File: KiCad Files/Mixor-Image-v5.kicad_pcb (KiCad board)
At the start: 2 copper layers, 60.6 x 46 mm, 83 parts, among them J1 Conn_01x03_Male, J2 Conn_01x03_Female, J3 Conn_01x03_Male, J4 Conn_01x03_Female, U1 TL072, U2 TL072

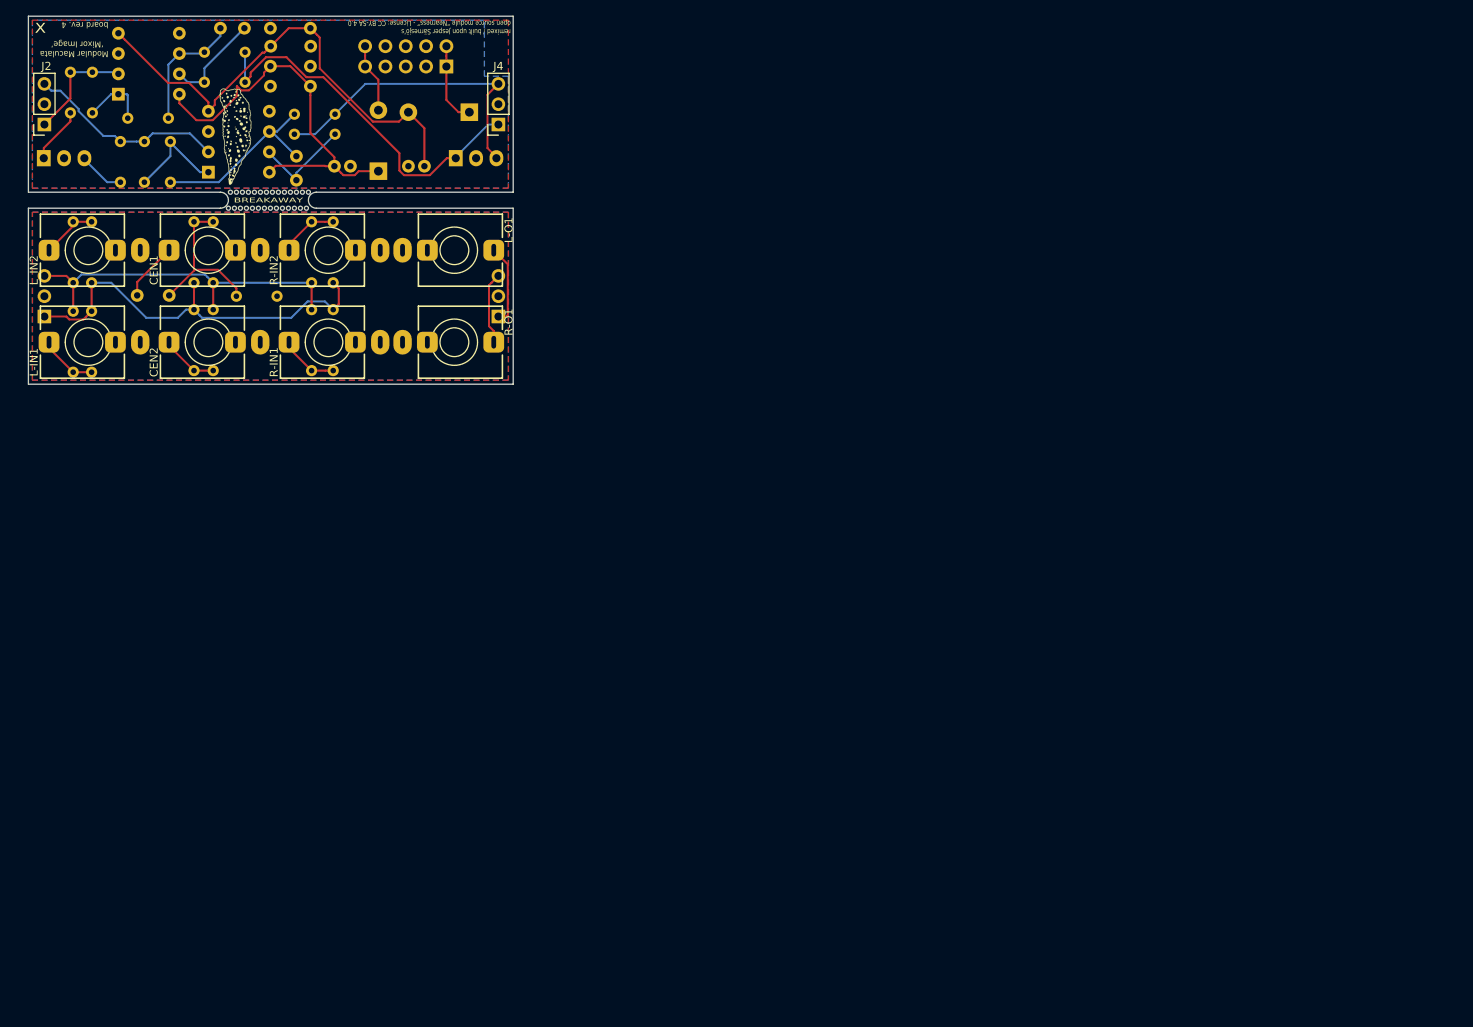
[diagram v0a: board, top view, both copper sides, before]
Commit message: remove Modular Maculata graphics
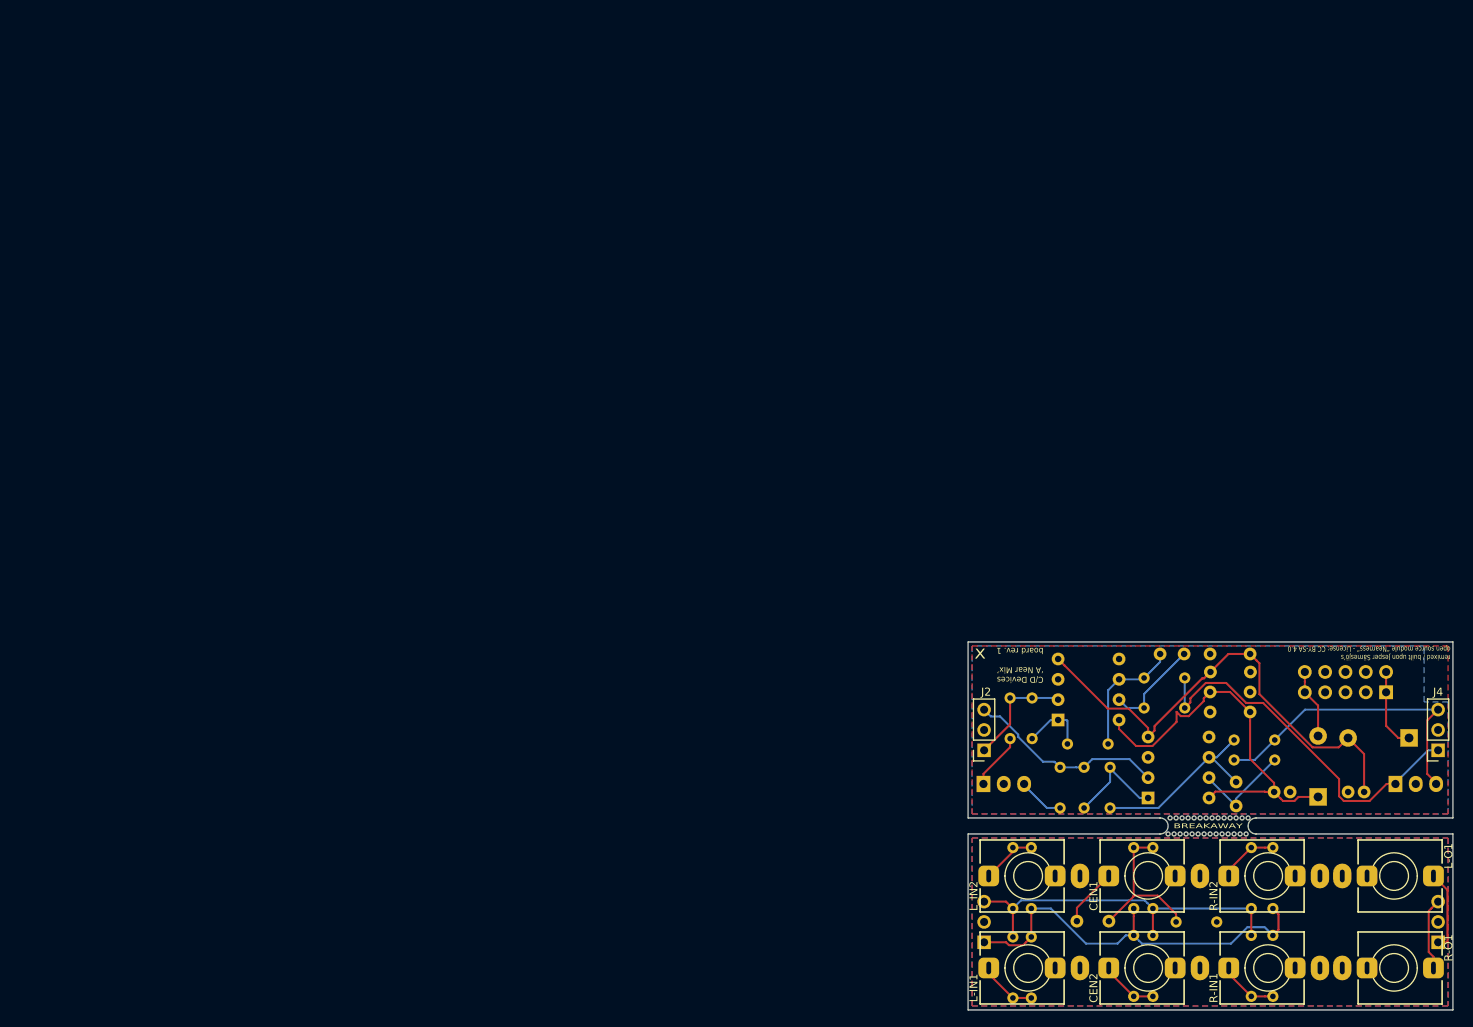
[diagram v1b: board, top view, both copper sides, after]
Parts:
- removed G*** (x2): LOGO, Nearness 1U:maculata_leaf_silk
- removed G*** (x2): LOGO, Nearness 1U:maculata_logo_copper
- removed the REF** at (25.0, 24.0)
- removed the REF** at (31.8, 24.0)
- removed the REF** at (32.5, 24.0)
- removed the REF** at (33.2, 24.0)
- removed the REF** at (34.0, 24.0)
- removed the REF** at (34.8, 24.0)
- removed the REF** at (35.0, 22.0)
- removed the REF** at (34.2, 22.0)
- removed the REF** at (33.5, 22.0)
- removed the REF** at (32.8, 22.0)
- removed the REF** at (32.0, 22.0)
- removed the REF** at (25.8, 24.0)
- removed the REF** at (31.2, 22.0)
- removed the REF** at (30.5, 22.0)
- removed the REF** at (29.8, 22.0)
- removed the REF** at (29.0, 22.0)
- removed the REF** at (28.2, 22.0)
- removed the REF** at (27.5, 22.0)
- removed the REF** at (26.8, 22.0)
- removed the REF** at (26.0, 22.0)
- removed the REF** at (26.5, 24.0)
- removed the REF** at (27.2, 24.0)
- removed the REF** at (28.0, 24.0)
- removed the REF** at (28.8, 24.0)
- removed the REF** at (29.5, 24.0)
- removed the REF** at (30.2, 24.0)
- removed the REF** at (31.0, 24.0)
- added REF**: 0.5mm_Hole, MountingHole:MountingHole_0.5mm, F.Cu at (143.2, 102.2)
- added REF**: 0.5mm_Hole, MountingHole:MountingHole_0.5mm, F.Cu at (147.0, 102.2)
- added REF**: 0.5mm_Hole, MountingHole:MountingHole_0.5mm, F.Cu at (145.7, 100.2)
- added REF**: 0.5mm_Hole, MountingHole:MountingHole_0.5mm, F.Cu at (151.7, 100.2)
- added REF**: 0.5mm_Hole, MountingHole:MountingHole_0.5mm, F.Cu at (144.7, 102.2)
- added REF**: 0.5mm_Hole, MountingHole:MountingHole_0.5mm, F.Cu at (149.5, 100.2)
- added REF**: 0.5mm_Hole, MountingHole:MountingHole_0.5mm, F.Cu at (145.0, 100.2)
- added REF**: 0.5mm_Hole, MountingHole:MountingHole_0.5mm, F.Cu at (151.0, 100.2)
- added REF**: 0.5mm_Hole, MountingHole:MountingHole_0.5mm, F.Cu at (146.2, 102.2)
- added REF**: 0.5mm_Hole, MountingHole:MountingHole_0.5mm, F.Cu at (148.0, 100.2)
- added REF**: 0.5mm_Hole, MountingHole:MountingHole_0.5mm, F.Cu at (142.5, 102.2)
- added REF**: 0.5mm_Hole, MountingHole:MountingHole_0.5mm, F.Cu at (148.7, 100.2)
- added REF**: 0.5mm_Hole, MountingHole:MountingHole_0.5mm, F.Cu at (146.5, 100.2)
- added REF**: 0.5mm_Hole, MountingHole:MountingHole_0.5mm, F.Cu at (147.2, 100.2)
- added REF**: 0.5mm_Hole, MountingHole:MountingHole_0.5mm, F.Cu at (152.5, 100.2)
- added REF**: 0.5mm_Hole, MountingHole:MountingHole_0.5mm, F.Cu at (150.2, 100.2)
- added REF**: 0.5mm_Hole, MountingHole:MountingHole_0.5mm, F.Cu at (149.2, 102.2)
- added REF**: 0.5mm_Hole, MountingHole:MountingHole_0.5mm, F.Cu at (150.7, 102.2)
- added REF**: 0.5mm_Hole, MountingHole:MountingHole_0.5mm, F.Cu at (151.5, 102.2)
- added REF**: 0.5mm_Hole, MountingHole:MountingHole_0.5mm, F.Cu at (147.7, 102.2)
- added REF**: 0.5mm_Hole, MountingHole:MountingHole_0.5mm, F.Cu at (143.5, 100.2)
- added REF**: 0.5mm_Hole, MountingHole:MountingHole_0.5mm, F.Cu at (150.0, 102.2)
- added REF**: 0.5mm_Hole, MountingHole:MountingHole_0.5mm, F.Cu at (148.5, 102.2)
- added REF**: 0.5mm_Hole, MountingHole:MountingHole_0.5mm, F.Cu at (145.5, 102.2)
- added REF**: 0.5mm_Hole, MountingHole:MountingHole_0.5mm, F.Cu at (152.2, 102.2)
- added REF**: 0.5mm_Hole, MountingHole:MountingHole_0.5mm, F.Cu at (144.0, 102.2)
- added REF**: 0.5mm_Hole, MountingHole:MountingHole_0.5mm, F.Cu at (144.2, 100.2)
- moved C1 141.1 mm to (131.1, 113.1)
- moved C2 141.1 mm to (141.5, 79.7)
- moved C3 141.1 mm to (151.0, 95.7)
- moved C4 141.1 mm to (155.7, 97.0)
- moved C5 141.1 mm to (165.0, 97.0)
- moved C6 141.1 mm to (152.7, 87.0)
- moved C7 141.1 mm to (152.8, 82.0)
- moved C8 141.1 mm to (147.7, 84.5)
- moved C9 141.1 mm to (147.7, 79.7)
- moved CEN1 141.1 mm to (140.0, 107.5)
- moved CEN2 141.1 mm to (140.0, 119.0)
- moved D1 141.1 mm to (161.2, 97.6)
- moved D2 141.1 mm to (172.6, 90.2)
- moved J1 141.1 mm to (119.5, 115.8)
- moved J2 141.1 mm to (119.5, 91.8)
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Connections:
- J1 pad 1: Net-(J1-Pad1) -> Net-(J1-Pin_1)
- J1 pad 3: Net-(J1-Pad3) -> Net-(J1-Pin_3)
- J3 pad 1: Net-(J3-Pad1) -> Net-(J3-Pin_1)
- J3 pad 3: Net-(J3-Pad3) -> Net-(J3-Pin_3)
- J4 pad 1: Net-(J4-Pad1) -> Net-(J4-Pin_1)
- J4 pad 3: Net-(J4-Pad3) -> Net-(J4-Pin_3)
- L-O1 pad T: Net-(J3-Pad1) -> Net-(J3-Pin_3)
- L-O1 pad TN: Net-(L-O1-PadTN) -> unconnected-(L-O1-PadTN)
- R-O1 pad T: Net-(J3-Pad3) -> Net-(J3-Pin_1)
- R-O1 pad TN: Net-(R-O1-PadTN) -> unconnected-(R-O1-PadTN)
- R10 pad 2: Net-(J1-Pad1) -> Net-(J1-Pin_3)
- R11 pad 2: Net-(J1-Pad3) -> Net-(J1-Pin_1)
- R12 pad 2: Net-(J1-Pad1) -> Net-(J1-Pin_3)
- R13 pad 2: Net-(J1-Pad3) -> Net-(J1-Pin_1)
- R14 pad 2: Net-(R14-Pad2) -> Net-(ST-IN1-Pin_3)
- R15 pad 1: Net-(R15-Pad1) -> Net-(ST-IN1-Pin_1)
- R2 pad 2: Net-(J1-Pad1) -> Net-(J1-Pin_3)
- R20 pad 2: Net-(J4-Pad1) -> Net-(J4-Pin_1)
- R21 pad 2: Net-(J4-Pad3) -> Net-(J4-Pin_3)
- R22 pad 2: Net-(J4-Pad1) -> Net-(J4-Pin_1)
- R23 pad 2: Net-(J4-Pad3) -> Net-(J4-Pin_3)
- R3 pad 2: Net-(J1-Pad3) -> Net-(J1-Pin_1)
- R4 pad 2: Net-(J1-Pad1) -> Net-(J1-Pin_3)
- R5 pad 2: Net-(J1-Pad3) -> Net-(J1-Pin_1)
- R6 pad 2: Net-(J1-Pad1) -> Net-(J1-Pin_3)
- R7 pad 2: Net-(J1-Pad3) -> Net-(J1-Pin_1)
- R8 pad 2: Net-(J1-Pad1) -> Net-(J1-Pin_3)
- R9 pad 2: Net-(J1-Pad3) -> Net-(J1-Pin_1)
- ST-IN1 pad 1: Net-(R14-Pad2) -> Net-(ST-IN1-Pin_1)
- ST-IN1 pad 3: Net-(R15-Pad1) -> Net-(ST-IN1-Pin_3)
- ST-OUT1 pad 1: Net-(J4-Pad1) -> Net-(J4-Pin_3)
- ST-OUT1 pad 3: Net-(J4-Pad3) -> Net-(J4-Pin_1)
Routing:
- net (no net): track 0.00 -> 213.9 mm
- net Net-(J1-Pad1): track 51.5 -> 0.00 mm
- net Net-(J4-Pad1): track 47.1 -> 0.00 mm
- net Net-(J1-Pad3): track 44.9 -> 0.00 mm
- net Net-(J4-Pad3): track 38.4 -> 0.00 mm
- net Net-(J3-Pad1): track 10.1 -> 0.00 mm
- net Net-(J3-Pad3): track 9.02 -> 0.00 mm
- net Net-(R14-Pad2): track 7.05 -> 0.00 mm
- net Net-(R15-Pad1): track 5.83 -> 0.00 mm
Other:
- net class Default removed
- board text added: "C/D Devices ‘A Near Mix’ board rev. 1"
- board text removed: "Modular Maculata ‘Mixor Image’ board rev. 4"

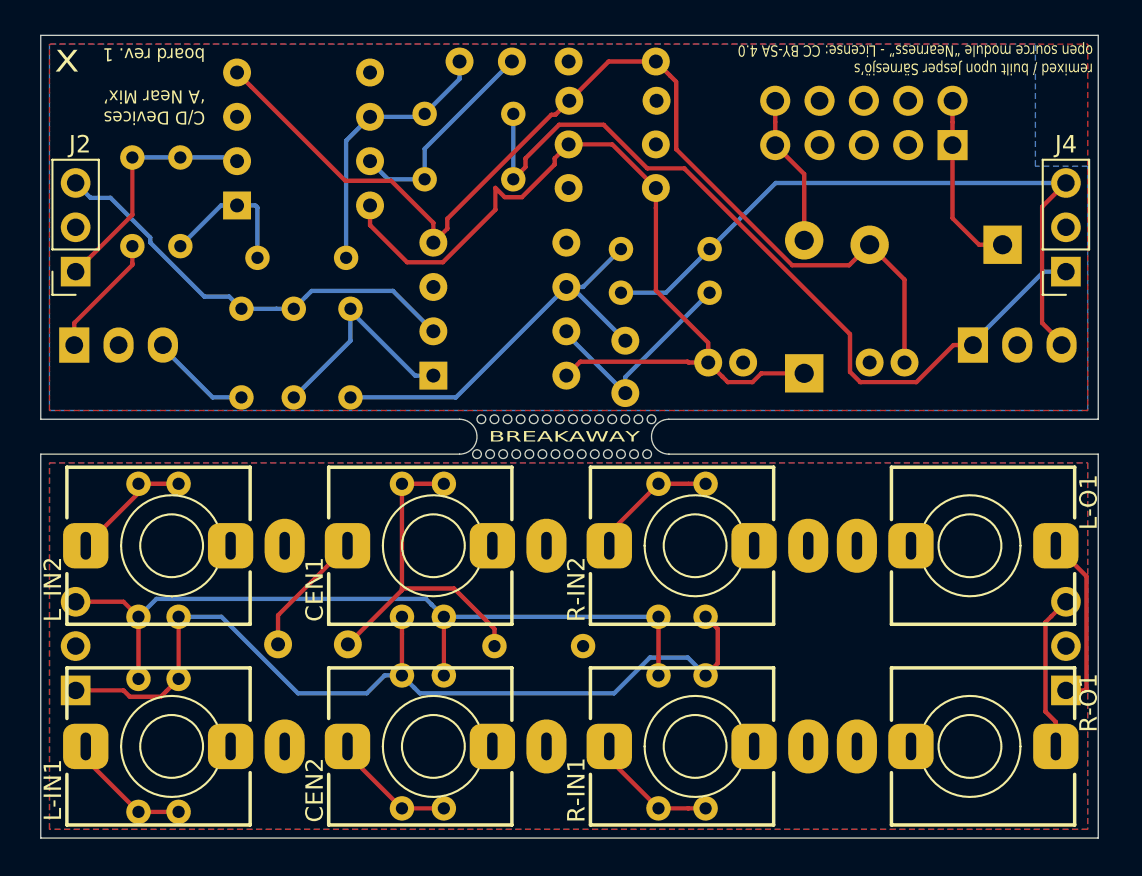
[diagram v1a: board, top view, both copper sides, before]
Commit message: adds C/D logo, change resistors to SMD
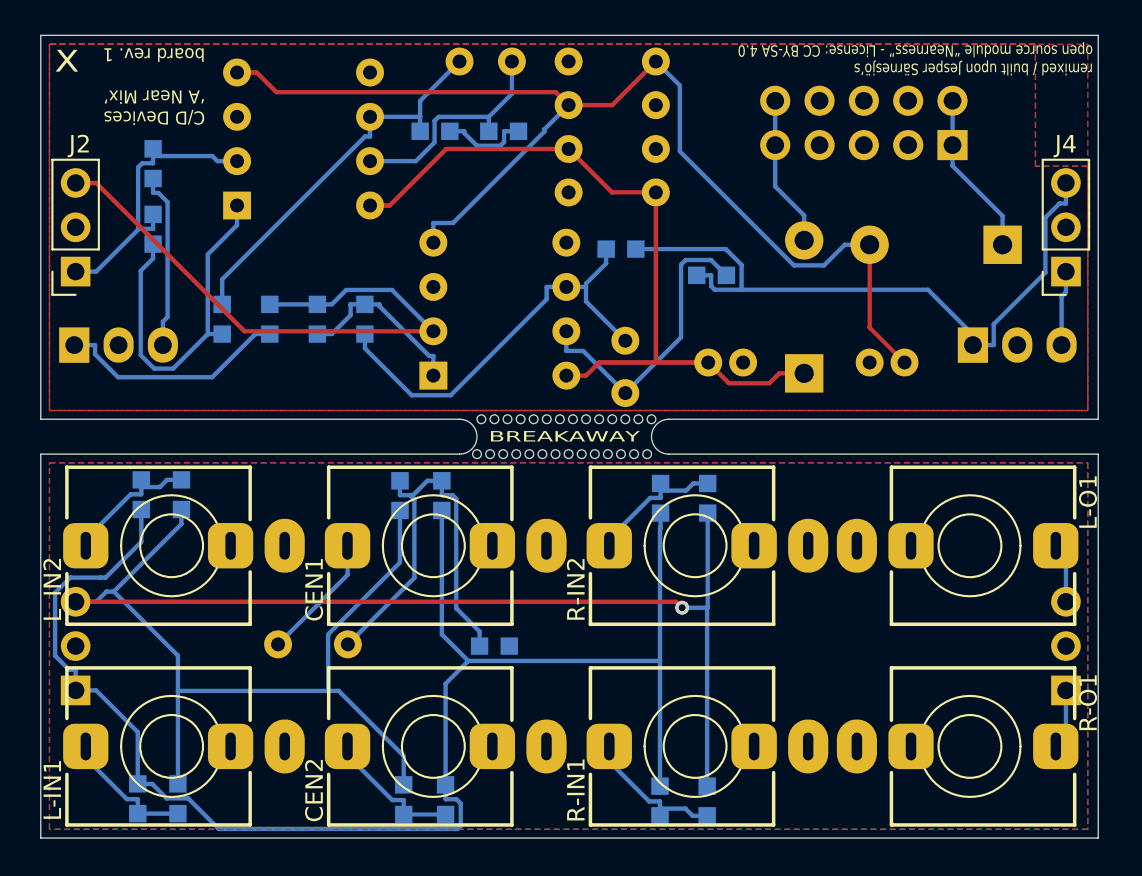
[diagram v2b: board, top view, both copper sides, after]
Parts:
- added logo: , Graphics, B.Cu at (124.8, 79.3)
- R1, R14, R15, R16, R17, R18, R19, R20, R21, R22, R23: footprint Resistor_THT:R_Axial_DIN0204_L3.6mm_D1.6mm_P5.08mm_Horizontal -> PCM_4ms_Resistor:R_0603
- R10, R11, R12, R13, R2, R3, R4, R5, R6, R7, R8, R9: footprint Resistor_THT:R_Axial_DIN0204_L3.6mm_D1.6mm_P7.62mm_Horizontal -> PCM_4ms_Resistor:R_0603
- moved R22 5.30 mm to (144.0, 83.7)
- moved R15 4.77 mm to (130.6, 94.5)
- moved R16 4.40 mm to (123.9, 89.3)
- moved R18 4.06 mm to (127.9, 94.5), turned to 90 degrees
- moved R17 1.48 mm to (133.3, 94.5)
- moved R14 1.24 mm to (123.9, 85.6)
- moved R20 1.16 mm to (140.1, 83.7)
- moved R19 1.02 mm to (136.0, 94.5)
- moved R23 1.00 mm to (155.9, 92.0)
- moved R12 0.84 mm to (155.7, 104.7)
- moved R13 0.84 mm to (153.0, 104.7)
- moved R4 0.75 mm to (125.3, 122.0)
- moved R5 0.75 mm to (123.0, 122.0)
- moved R6 0.69 mm to (138.0, 104.6)
- moved R7 0.69 mm to (140.4, 104.6)
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- renumbered REF** to MOUSE_BITE_01, REF** to MOUSE_BITE_02, REF** to MOUSE_BITE_03, REF** to MOUSE_BITE_04, REF** to MOUSE_BITE_05, REF** to MOUSE_BITE_06, REF** to MOUSE_BITE_07, REF** to MOUSE_BITE_08, REF** to MOUSE_BITE_09, REF** to MOUSE_BITE_10, REF** to MOUSE_BITE_11, REF** to MOUSE_BITE_12, REF** to MOUSE_BITE_13, REF** to MOUSE_BITE_14, REF** to MOUSE_BITE_15, REF** to MOUSE_BITE_16, REF** to MOUSE_BITE_17, REF** to MOUSE_BITE_18, REF** to MOUSE_BITE_19, REF** to MOUSE_BITE_20, REF** to MOUSE_BITE_21, REF** to MOUSE_BITE_22, REF** to MOUSE_BITE_23, REF** to MOUSE_BITE_24, REF** to MOUSE_BITE_25, REF** to MOUSE_BITE_26, REF** to MOUSE_BITE_27, REF** to MOUSE_BITE_28
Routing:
- net (no net): track 213.9 -> 0.00 mm
- net Net-(J1-Pin_3): track 0.00 -> 101.5 mm, vias 0 -> 1
- net Net-(J1-Pin_1): track 0.00 -> 88.1 mm
- net Net-(J4-Pin_3): track 0.00 -> 38.7 mm
- net Net-(ST-IN1-Pin_1): track 0.00 -> 13.3 mm
- net Net-(R16-Pad2): track 8.31 -> 20.5 mm
- net Net-(ST-IN1-Pin_3): track 0.00 -> 10.2 mm
- net Net-(J2-Pin_3): track 25.0 -> 34.7 mm
- net Net-(J4-Pin_1): track 0.00 -> 9.36 mm
- net Net-(U1B--): track 15.7 -> 22.2 mm
- net +12V: track 49.5 -> 43.2 mm
- net Net-(C3-Pad2): track 12.7 -> 17.3 mm
- net Net-(C1-Pad2): track 20.1 -> 24.5 mm
- net -12V: track 60.7 -> 64.9 mm
- net Net-(J3-Pin_3): track 0.00 -> 3.45 mm
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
